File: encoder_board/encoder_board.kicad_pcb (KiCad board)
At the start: 2 copper layers, 48 x 16 mm, 4 parts, among them J1 Conn_01x06, U1 AS5048A

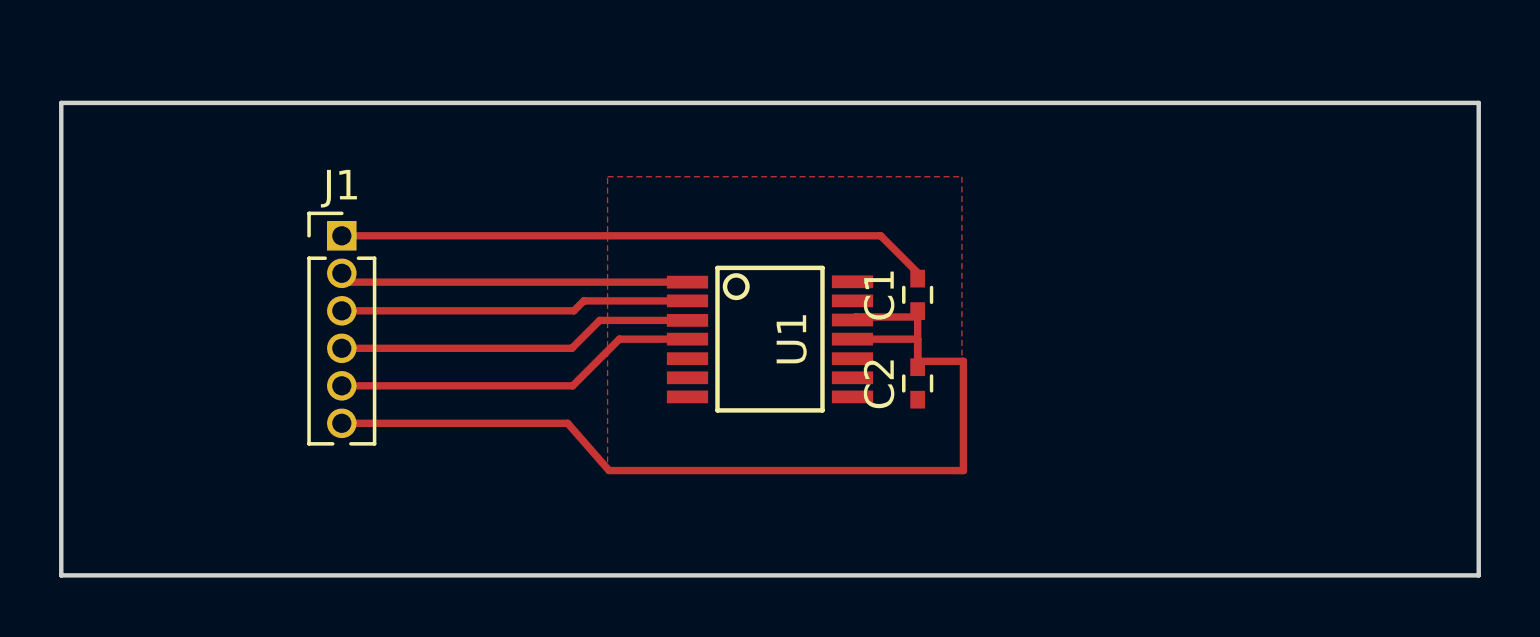
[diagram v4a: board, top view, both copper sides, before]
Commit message: redo pcb shape to match CAD changes
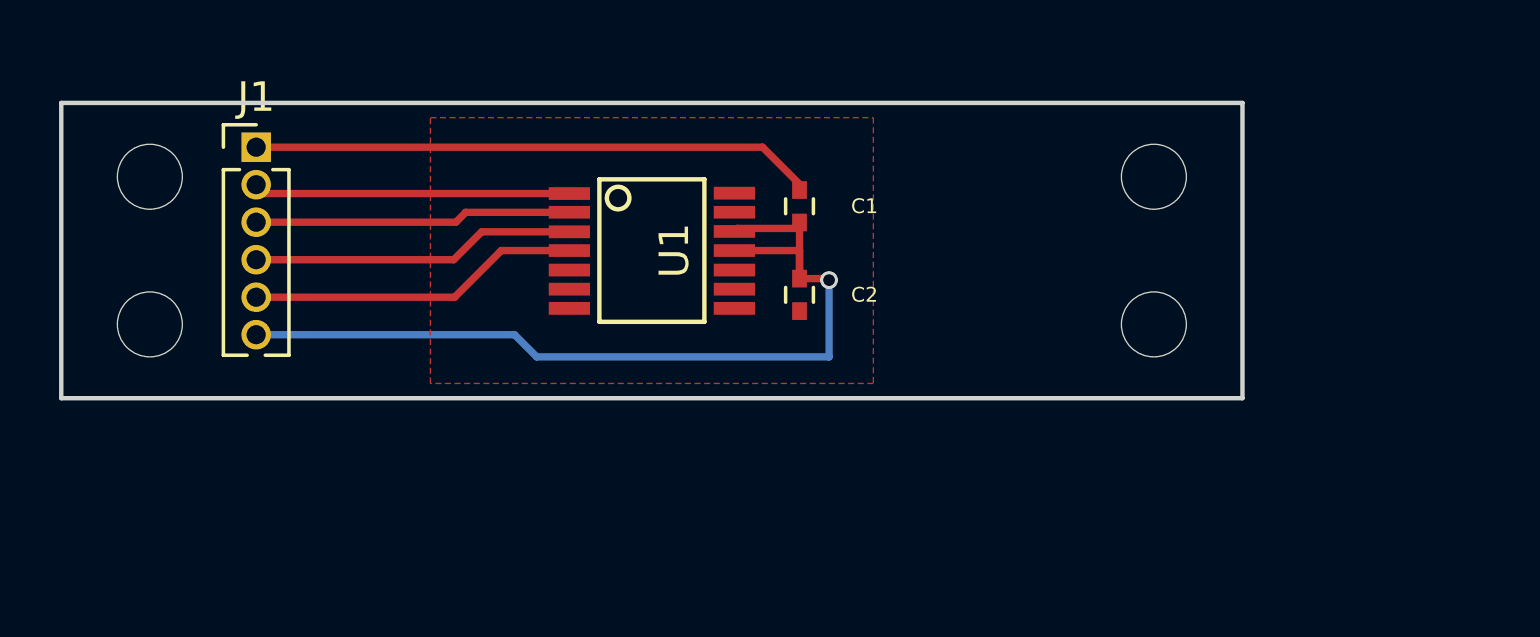
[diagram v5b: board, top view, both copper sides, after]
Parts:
- added REF**: MountingHole_2.2mm_M2, Mounting_Holes:MountingHole_2.2mm_M2, F.Cu at (103.0, 102.5)
- added REF**: MountingHole_2.2mm_M2, Mounting_Holes:MountingHole_2.2mm_M2, F.Cu at (103.0, 107.5)
- added REF**: MountingHole_2.2mm_M2, Mounting_Holes:MountingHole_2.2mm_M2, F.Cu at (137.0, 107.5)
- added REF**: MountingHole_2.2mm_M2, Mounting_Holes:MountingHole_2.2mm_M2, F.Cu at (137.0, 102.5)
- moved C1 5.00 mm to (125.0, 103.5)
- moved C2 5.00 mm to (125.0, 106.5)
- moved U1 5.00 mm to (120.0, 105.0)
- moved J1 4.17 mm to (106.6, 101.5)
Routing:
- net +3V3: track 33.9 -> 30.9 mm, vias 0 -> 1
- net CS: track 11.8 -> 10.7 mm
- net CLK: track 11.8 -> 10.7 mm
- net MOSI: track 12.4 -> 11.3 mm
- net MISO: track 12.1 -> 11.0 mm
- net GND: track 20.0 -> 18.9 mm
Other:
- board size 48 x 16 mm -> 40 x 10 mm
